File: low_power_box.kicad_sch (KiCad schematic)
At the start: 7 parts

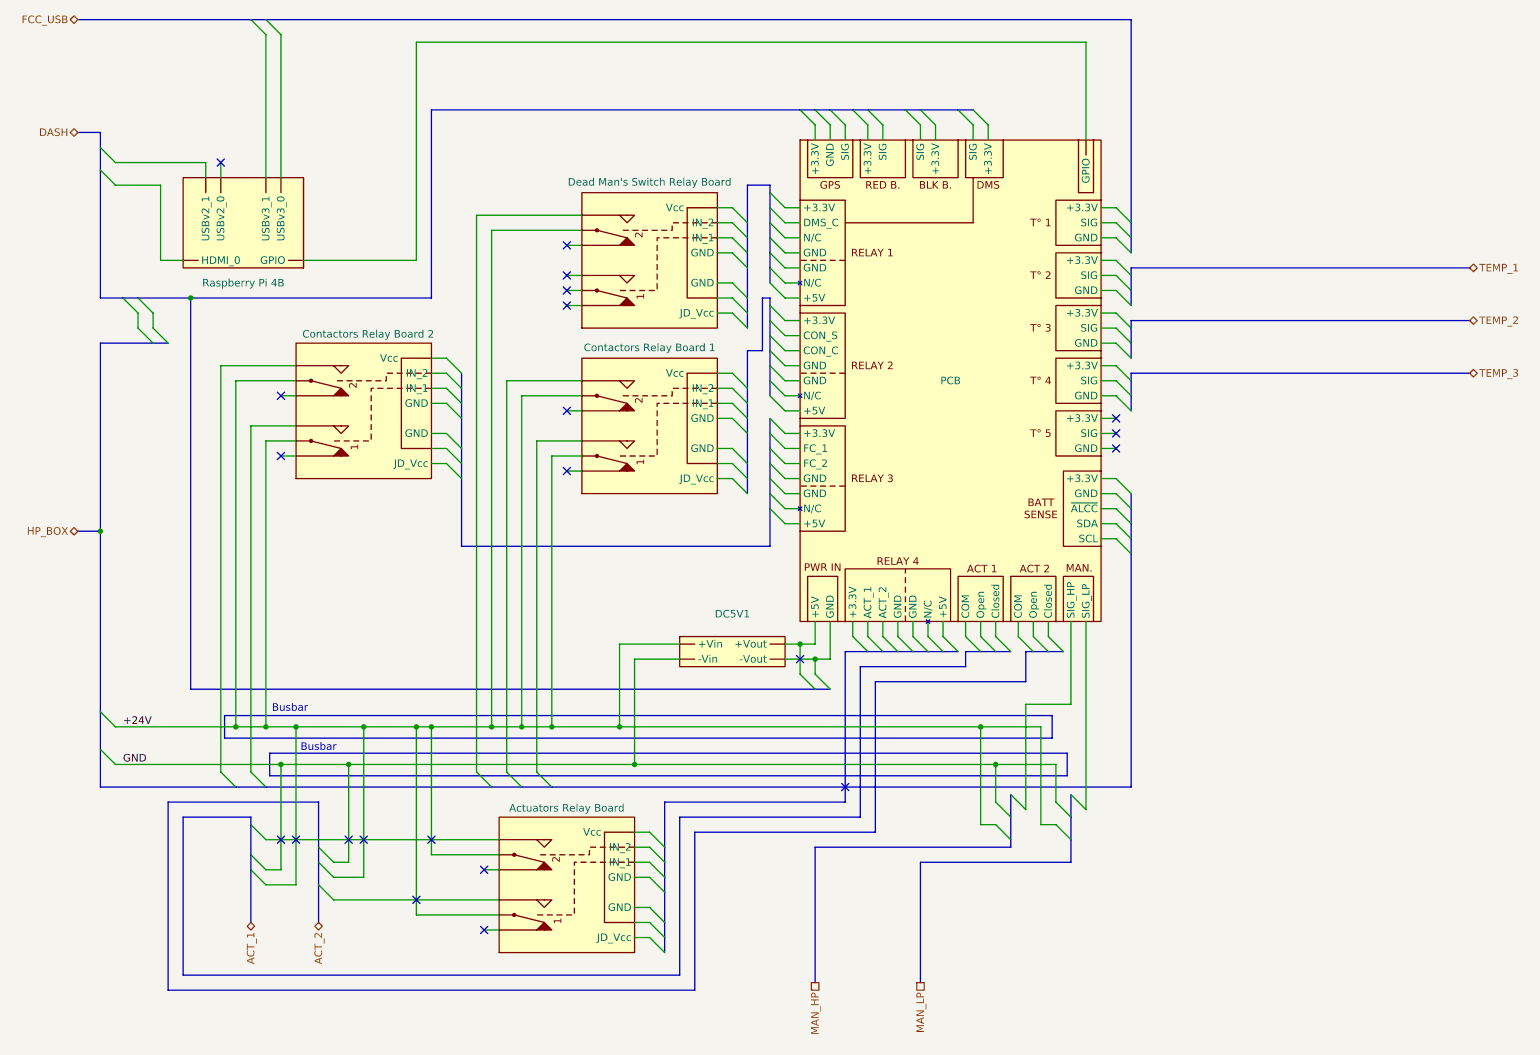
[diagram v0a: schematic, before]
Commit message: Add labels
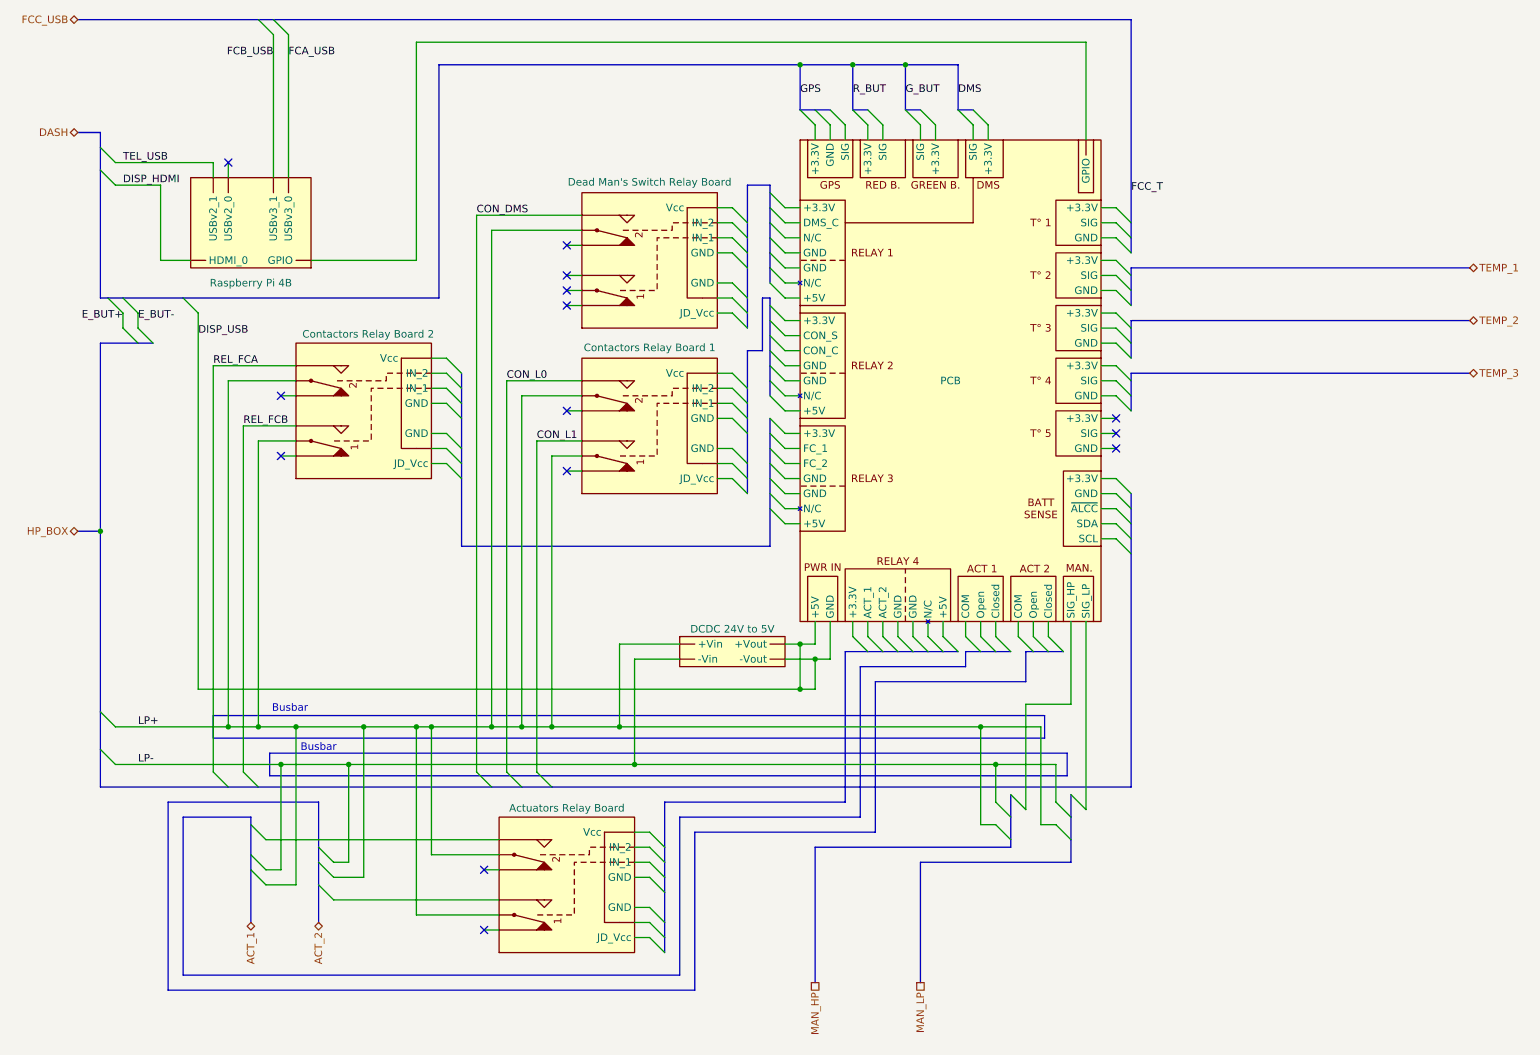
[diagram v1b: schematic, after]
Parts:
- DCDC5V: renamed from DC5V1; Name (none) -> DCDC 24V to 5V
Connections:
- net GND is gone; now on net LP-: DCDC5V. (-Vout)
- net REL_FCB: now reaches RELB1. (Vcc)
- net LP+: now reaches RELB2. (Vcc)
- net LP+: now also DCDC5V. (-Vout), RELB1. (Vcc), RELB3. (Vcc), RELB4. (Vcc)
- net DISP_USB: now reaches DCDC5V. (-Vout), PCB1. (~{ALCC})
- net LP-: now reaches DCDC5V. (-Vout)
- net LP-: no longer PCB1. (~{ALCC})
- net TEL_USB: now reaches RPI1. (USBv3_1)
- removed net +24V: DCDC5V. (-Vout), RELB1. (Vcc), RELB2. (Vcc), RELB3. (Vcc), RELB4. (Vcc)
- new net: PCB1. (~{ALCC}), RPI1. (USBv3_1)
- new net CON_DMS: RELB4. (Vcc)
- new net CON_L0: RELB3. (Vcc)
- new net CON_L1: RELB3. (Vcc)
- new net DISP_HDMI: RPI1. (USBv3_1)
- new net FCA_USB: RPI1. (USBv3_1)
- new net FCB_USB: RPI1. (USBv3_1)
- new net REL_FCA: RELB1. (Vcc)
- no-connect marks 22 -> 14
